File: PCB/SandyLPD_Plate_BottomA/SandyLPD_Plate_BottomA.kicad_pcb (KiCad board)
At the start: 2 copper layers, 127.4 x 83 mm, 14 parts

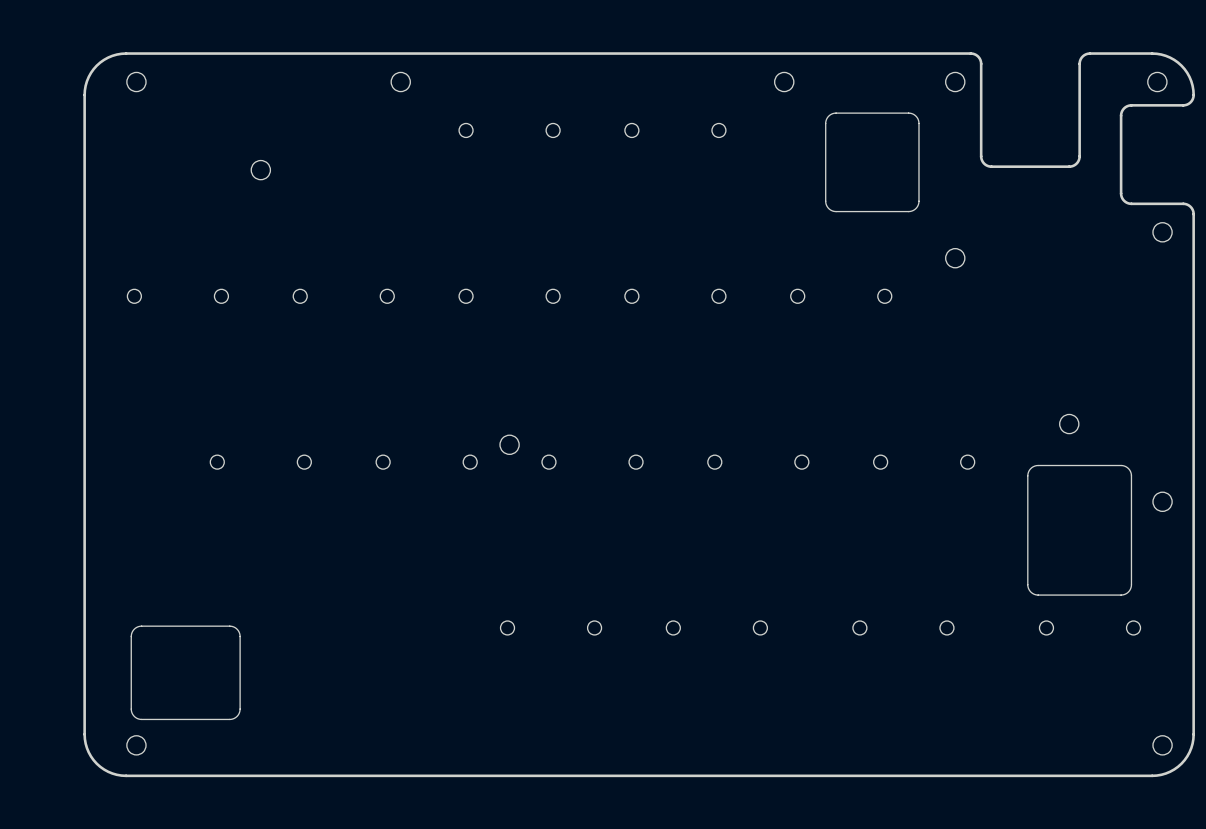
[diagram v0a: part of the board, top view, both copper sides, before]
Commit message: ボトムプレートの外形を、基板Baseと同形状に戻す。
仕様では左右端を斜めにして、テント時の小指側持ち上がりを防止する予定だった。
しかし、ケースなどを考慮すると、ボトムの外形が異なると不都合なため、基板Baseと同形状とする。
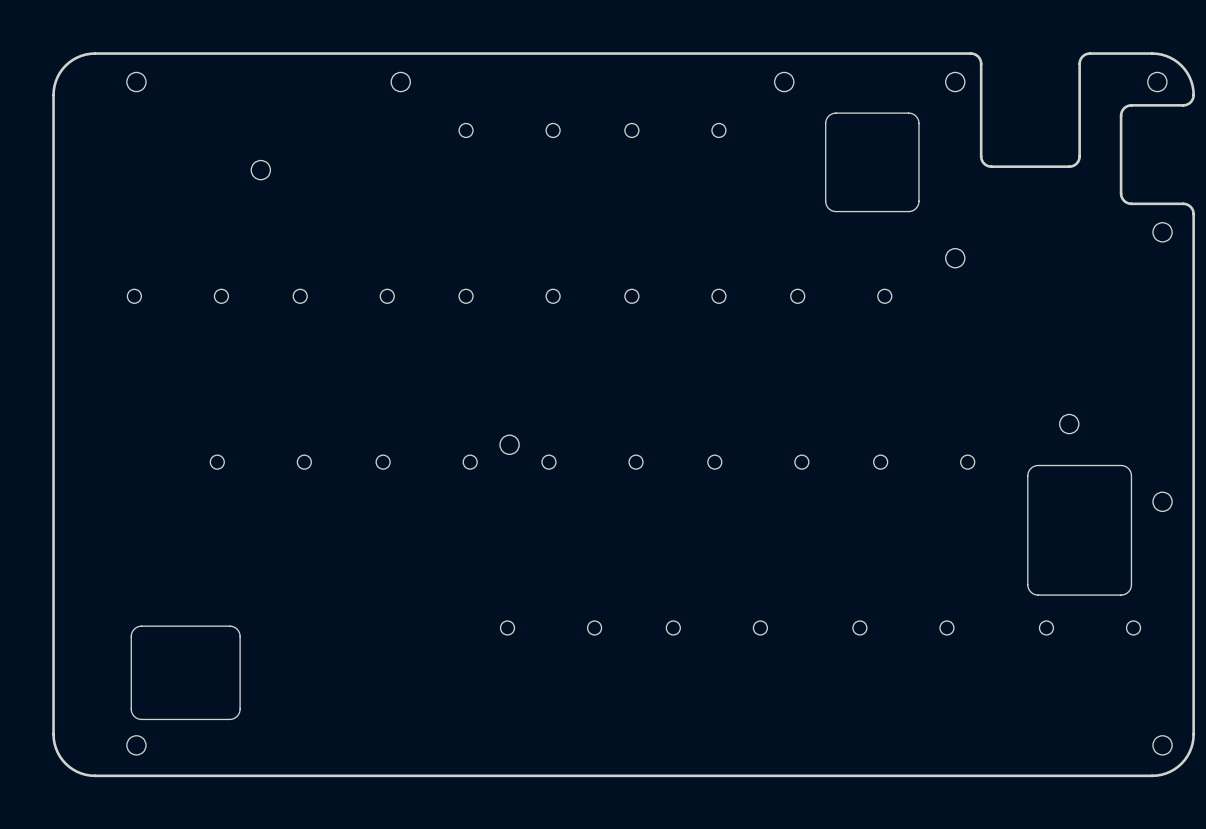
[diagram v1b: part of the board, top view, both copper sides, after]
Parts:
- REF**: footprint locallib:SandyLP-Duo_outline_BottomA_narrow_edge -> locallib:SandyLP-Duo_outline_BottomA
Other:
- board size 127.4 x 83 mm -> 131 x 83 mm
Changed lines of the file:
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@@
 		)
 	)
-	(footprint "locallib:SandyLP-Duo_outline_BottomA_narrow_edge"
+	(footprint "locallib:SandyLP-Duo_outline_BottomA"
 		(locked yes)
 		(layer "F.Cu")
@@
 			)
 		)
-		(property "Footprint" "locallib:SandyLP-Duo_outline_BottomA_narrow_edge"
+		(property "Footprint" "locallib:SandyLP-Duo_outline_BottomA"
 			(at 2.38125 0 0)
 			(layer "F.Fab")
@@
 		)
 		(property "LCSC-Reserve" ""
-			(at 125.015625 11.015585 0)
+			(at -97.63125 19.05 90)
 			(unlocked yes)
 			(layer "B.Fab")
@@
 		)
 		(property "text" "RESET"
-			(at 127.015625 12.715585 0)
+			(at -97.63125 22.50661 180)
 			(unlocked yes)
 			(layer "B.SilkS")
@@
 			(effects
 				(font
-					(size 0.8 0.8)
-					(thickness 0.12)
+					(size 1 1)
+					(thickness 0.15)
 				)
-				(justify right mirror)
+				(justify mirror)
 			)
 		)
@@
 			)
 		)
-		(attr through_hole)
+		(attr through_hole board_only)
 		(fp_line
 			(start -140.49375 -66.675)
@@
 		)
 		(fp_line
-			(start -132.159486 26.123471)
-			(end -132.159486 -47.32504)
+			(start -135.731364 26.123471)
+			(end -135.731364 -47.32504)
 			(stroke
 				(width 0.3)
@@
 		(fp_line
 			(start -30.360962 -52.08754)
-			(end -127.396986 -52.08754)
+			(end -130.968864 -52.08754)
 			(stroke
 				(width 0.3)
@@
 		(fp_line
 			(start -9.525004 30.885971)
-			(end -127.396986 30.885971)
+			(end -130.968864 30.885971)
 			(stroke
 				(width 0.3)
@@
 		)
 		(fp_arc
-			(start -132.159486 -47.32504)
-			(mid -130.764582 -50.692636)
-			(end -127.396986 -52.08754)
+			(start -135.731364 -47.32504)
+			(mid -134.33646 -50.692636)
+			(end -130.968864 -52.08754)
 			(stroke
 				(width 0.3)
@@
 		)
 		(fp_arc
-			(start -127.396986 30.885971)
-			(mid -130.764582 29.491067)
-			(end -132.159486 26.123471)
+			(start -130.968864 30.885971)
+			(mid -134.33646 29.491067)
+			(end -135.731364 26.123471)
 			(stroke
 				(width 0.3)
@@
 		)
 		(group ""
-			(members "005edbd5-9dcd-470a-a973-d1f1d2a61a1a" "05d2eae7-c181-422d-9569-904796de0269"
-				"9b183af6-5e10-4e59-8052-0b5744671b76" "b55f851b-591d-4a62-a20e-bd009cb65a13"
-			)
-		)
-		(group ""
-			(members "42a0653b-d340-4603-a827-220ef89f28cc" "850d6d43-24ba-41c6-9baf-5d99699f05ff")
-		)
-		(group ""
-			(members "00bba4d7-927c-44bf-abe4-f5398d7c5d70" "3fc21fe5-b83e-4190-8479-5b87a99d230f"
-				"5695b5e9-40c7-4808-97a4-c3f6905e49b1" "98fb170c-914d-4c2a-b8dc-1b4193d5b75c"
-			)
-		)
-		(group ""
-			(members "2114cb56-aaf9-424c-958d-764355443606" "22d33ce8-87ca-4359-a9de-ef28831f7c19"
-				"351bab31-3389-412d-acae-cb307b4c7e3e" "eb69ca11-c496-4460-b676-2f4452785759"
-			)
-		)
-		(group ""
-			(members "0047b21b-dea4-4b7c-ad55-e57c259c307c" "29b073e0-2a04-4572-8567-e3811bda6a15"
-				"77b25d4e-8323-4d78-971c-3cebbb8b50fd"
-			)
-		)
-		(group ""
-			(members "30b09278-b5c3-452a-9b74-d88fc7e4de33" "9bb58a16-0232-48a8-8b61-7405ef1a8437"
-				"c234e008-7641-4094-bf84-fe76896330e9"
-			)
-		)
-		(group ""
-			(members "27051af8-4828-47fd-bd2c-5783529d2d3c" "4f6412f7-2e76-4052-b919-9ae8df068e09"
-				"da862006-59d0-48f0-af84-c2b3950611b3"
-			)
-		)
-		(group ""
-			(members "4e68ace4-0a08-4553-a9ea-0aca04e8a678" "8083394e-fa4c-4ab0-9e85-c20af4f6b881"
-				"f871543f-5335-4d4e-a8c8-eb321251eed3"
-			)
-		)
-		(group ""
-			(members "162c7e05-0cab-437d-964e-3a034e5c93db" "27b03c83-74c5-462a-8bb9-f4302292ff28"
-				"94b7f3ef-9673-44e5-82e3-eb0b3f6f3867"
-			)
-		)
-		(group ""
-			(members "83e13a7e-7942-444c-b689-bfa5e10521b8" "8f398c76-707b-4463-be56-22b0d8080667"
-				"e7605193-7462-471f-979d-74e4487fd460"
-			)
-		)
-		(group ""
-			(members "4f8089c0-3afb-49d3-8d5a-00519c085a6d" "657a6b24-7aa7-4307-ab6f-31d937f6afff"
-				"c17c0421-2946-4162-9b96-5a1f954f5d27"
-			)
-		)
-		(group ""
-			(members "20ce9a84-afb0-4c77-b779-3d139d9c7c1d" "a4a9556f-885c-41b6-bd16-850c0e5a4910"
-				"c1f55ea5-07ff-4878-bbb3-28cd7b18d6e4"
-			)
-		)
-		(group ""
-			(members "990a4551-984d-4bbe-8049-91a3043cd0b8" "cf7cfe3b-81bb-490e-85b5-f96267643e1b"
-				"f8a0acfc-dc36-4631-84b4-7c14b025cac1"
-			)
-		)
-		(group ""
-			(members "71f33917-bf52-475a-96be-18edf2ad2e9b" "c20582ea-7f0c-447c-91e7-f06e8854089a"
-				"e2f5758b-f261-41e1-bf9b-ea9e8c73e7c5"
-			)
-		)
-		(group ""
-			(members "24957f64-19f9-4ebe-af70-10ff27c7b894" "5c667c15-8fa1-40d5-8bb5-5f8ca7b33a4f"
-				"bde45b41-1ed9-4ff2-a4a1-598ec35577d0"
-			)
-		)
-		(group ""
-			(members "4b262687-535b-4b71-b50e-c1b3c09d4763" "6457ffeb-18c2-4019-942c-4b4097e8bd1e"
-				"7a08e892-188a-4d2b-b535-3c2151e6a3cb"
-			)
-		)
-		(group ""
-			(members "0ba3edbb-be55-4cc1-8689-aa70d6c0190d" "653fb40f-2811-46bd-a5b8-fef2f5af4ec3"
-				"f404e5fb-4055-419b-a6f1-4105c89f8d55"
-			)
-		)
-		(group ""
-			(members "09f0a9b0-09f9-4392-8691-bb053f5843d8" "346f39a6-52ef-4b8d-b4cc-c828106052b7"
-				"4f1562ec-583d-4b9e-913d-2068b0b31fe3" "9f233960-38e7-4d17-8b07-61f26d310015"
-				"a5ed21ac-c260-4b32-9b59-175a99054753" "ceb8e2f6-c06f-4b01-ac69-351496e250e1"
-				"fc590dfd-88df-4a9d-94aa-c44babb90b2a"
-			)
-		)
+			(members "768d52e1-6995-4e07-a8f7-905398240928" "7c9ff0f7-4d82-402f-bc0a-521dbdc4ffab"
+				"c7a505ad-1373-40c9-8598-3adb5f37292c" "d3a47df1-53fc-47b6-bce4-7b199c321008"
+			)
+		)
+		(group ""
+			(members "27b3e30e-4b55-4486-b54d-d5f02c1e864f" "47688318-7972-4377-adad-ed33bbecca86"
+				"61592db4-dc05-4c05-867c-43a3c4575e85" "ab165d60-8426-4dda-93f6-c43c93c70db7"
+			)
+		)
+		(group ""
+			(members "050ef1a6-a3f2-433d-ba6f-f7bf6cbc7701" "266b9d01-f5d8-45c4-a070-ecec62cbbcd0"
+				"3fd5bdf2-c0fe-45b4-ab12-3b4e4d8df1f7" "6698c4d4-7943-4c04-8872-1a55fe845aab"
+			)
+		)
+		(group ""
+			(members "120b0628-372f-493f-b00e-15f3ba5435f2" "b84d7721-bd67-439d-8f72-ec4f61046289")
+		)
+		(group ""
+			(members "0b69fad6-0d2d-46c8-8b7f-c6ae73ae9535" "330257f5-ee5d-4c76-80d8-5f791fdf178f"
+				"e02aad9b-a0a9-48c2-aac7-61630aa05e4b"
+			)
+		)
+		(group ""
+			(members "0a2b1baf-e4ce-4170-b5fe-0cd55f32a29b" "4c80776c-a1aa-4eac-a4f0-7c2fa99df76c"
+				"9b2fab13-b30c-465b-b73c-f1cb87b9b07d"
+			)
+		)
+		(group ""
+			(members "3cc7c1a2-46e7-43fa-8d77-b0583e360804" "9993816f-2ec5-4f18-8ccb-fa76e125fbf3"
+				"c0989285-ddbc-48e9-bfa8-efb41389e4ee"
+			)
+		)
+		(group ""
+			(members "6a4246bb-16fd-4932-8b00-0759913a3d4d" "7369f70d-806d-4907-98e3-015ef96cb96d"
+				"7bb1f348-f5a8-4d84-aa64-cfe7065df81c"
+			)
+		)
+		(group ""
+			(members "2cd84ebf-6e32-4566-8d34-cbd5c0dce843" "ac2ea378-a8dc-4c2b-8970-88981ff65753"
+				"b4734dbe-c653-43f4-8039-96a65bf3900d"
+			)
+		)
+		(group ""
+			(members "12e533cc-6258-43f2-9c2e-665cb9adc7f7" "1f986533-4d05-4a11-9c0a-8a3708b5372b"
+				"931a2f65-5bcb-44d3-b7dd-751c7b60f58b"
+			)
+		)
+		(group ""
+			(members "2611aa98-c19b-4191-9a14-da2c351c2c8c" "7c83b1d8-b4a3-49de-83ec-d4ebc99a612e"
+				"c12838cb-8578-4aa5-b47d-60ebd0292c47"
+			)
+		)
+		(group ""
+			(members "af508a5a-8108-4dad-8260-e2b96960a5a1" "af604911-4095-4891-a997-ae5661578ee4"
+				"dacfb637-0ed1-493e-93e5-c88e1ac657cb"
+			)
+		)
+		(group ""
+			(members "127c6c8f-8dc6-4082-9bb4-d7a6a6d983af" "1365b648-5cb8-4079-bcc7-22ed2e8a1f14"
+				"f56c55e2-61a0-4616-9f47-95582bca677a"
+			)
+		)
+		(group ""
+			(members "5a9f1272-29aa-498f-aac3-a79cfba13a0f" "8d27a991-15c2-4cf6-8f08-53455c4a44d3"
+				"bcdf979c-70a9-4690-9902-d5d13f43a3ff"
+			)
+		)
+		(group ""
+			(members "341c500e-d4b8-4c4d-aff6-785cf25e11de" "44107841-d251-407a-9a46-594b2a54cde6"
+				"86f19132-709f-4b84-827d-3de39abfd1b1"
+			)
+		)
+		(group ""
+			(members "5b0d7b5c-7741-4c0a-83dd-f11fbcda69bb" "638280cb-4e4f-4d5d-a0ad-a617928cc635"
+				"96436da2-e83e-4c46-a5ea-b19277da9758"
+			)
+		)
+		(group ""
+			(members "1fb38e07-3180-42ea-b84e-b8959f434f60" "af95d0d9-5dfa-4313-b6c6-74592eeea5cf"
+				"bb264223-f065-43ed-a360-1068521864a8"
+			)
+		)
+		(group ""
+			(members "099a1441-f742-4c18-bcac-b4f41b16570d" "1c8e6033-ca91-4b2b-90ca-e53cea9a4255"
+				"1cbb4c32-75d4-4e97-a4f2-0c4f3be2bba7" "5f7d4a69-8910-41d2-a414-02484530e2fb"
+				"99a17b21-8b5f-46dc-8c4d-2b70c8e77b8d" "ac859754-1366-4110-973d-db881cdbc23a"
+				"c2c4e08e-bcca-4d8f-ab7d-31ca58c78905"
+			)
+		)

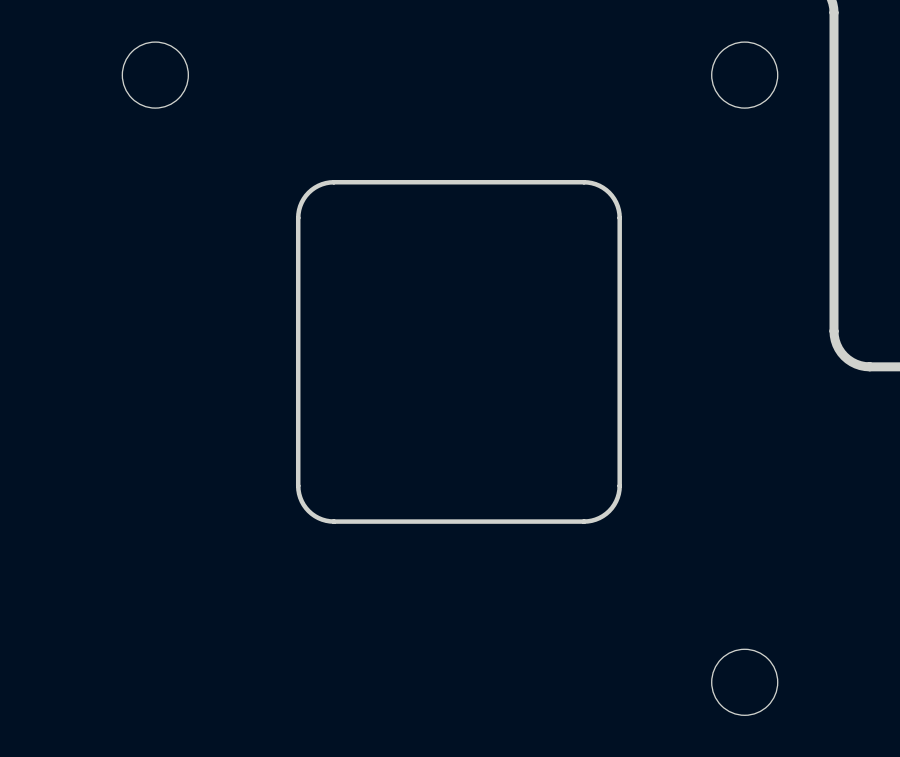
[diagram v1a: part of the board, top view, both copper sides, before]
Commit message: 部品逃がし穴の位置とサイズを調整
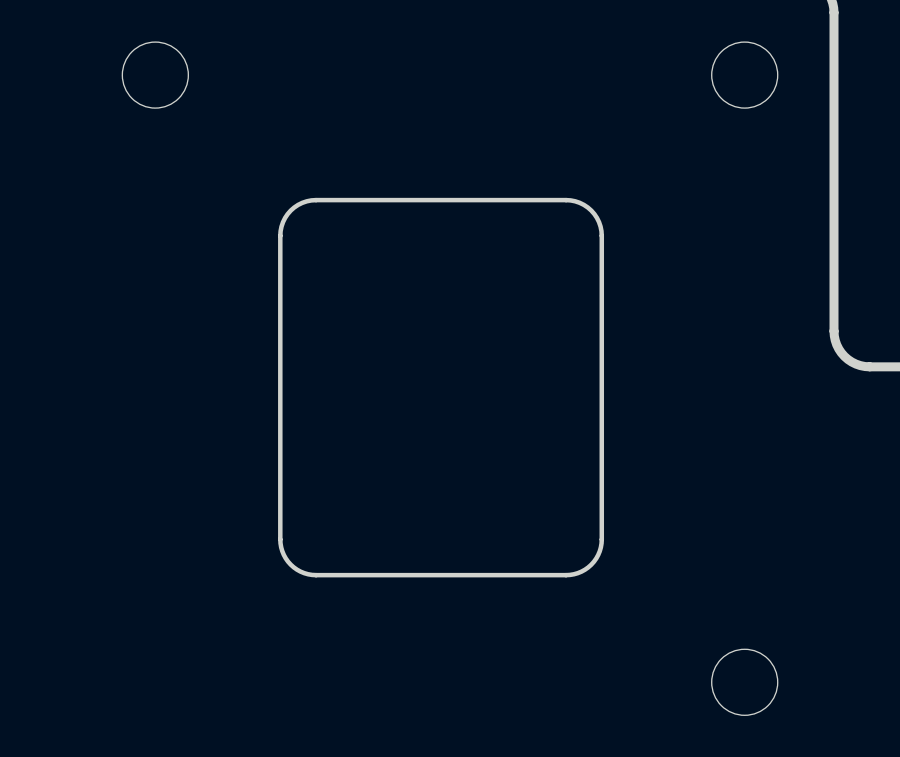
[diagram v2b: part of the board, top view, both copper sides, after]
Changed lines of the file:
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@@
+		(layer "Eco2.User")
+	)
+	(gr_rect
+		(start 111.543804 39.50499)
+		(end 122.259477 51.41125)
+		(stroke
+			(width 0.1)
+			(type default)
+		)
+		(fill none)
 		(layer "Eco2.User")
 	)
@@
 		(layer "Edge.Cuts")
 	)
-	(gr_line
-		(start 112.141322 40.100289)
-		(end 112.141322 49.029984)
-		(locked yes)
-		(stroke
-			(width 0.15)
-			(type default)
-		)
-		(layer "Edge.Cuts")
-	)
-	(gr_line
-		(start 122.856956 49.029984)
-		(end 122.856956 40.100289)
-		(locked yes)
-		(stroke
-			(width 0.15)
-			(type default)
-		)
-		(layer "Edge.Cuts")
-	)
 	(gr_arc
 		(start 147.264789 93.083146)
@@
 		(layer "Edge.Cuts")
 	)
-	(gr_arc
-		(start 112.141322 40.100289)
-		(mid 112.490048 39.258389)
-		(end 113.331948 38.909663)
-		(locked yes)
-		(stroke
-			(width 0.15)
-			(type default)
-		)
-		(layer "Edge.Cuts")
-	)
-	(gr_arc
-		(start 121.66633 38.909663)
-		(mid 122.50823 39.258389)
-		(end 122.856956 40.100289)
-		(locked yes)
-		(stroke
-			(width 0.15)
-			(type default)
-		)
-		(layer "Edge.Cuts")
-	)
-	(gr_line
-		(start 121.66633 50.22061)
-		(end 113.331948 50.22061)
+	(gr_line
+		(start 122.259611 40.695531)
+		(end 122.259611 50.815579)
+		(locked yes)
+		(stroke
+			(width 0.15)
+			(type default)
+		)
+		(layer "Edge.Cuts")
+	)
+	(gr_arc
+		(start 111.543977 40.695531)
+		(mid 111.89271 39.853655)
+		(end 112.734603 39.504905)
+		(locked yes)
+		(stroke
+			(width 0.15)
+			(type default)
+		)
+		(layer "Edge.Cuts")
+	)
+	(gr_arc
+		(start 121.068985 39.504905)
+		(mid 121.910869 39.853641)
+		(end 122.259611 40.695531)
+		(locked yes)
+		(stroke
+			(width 0.15)
+			(type default)
+		)
+		(layer "Edge.Cuts")
+	)
+	(gr_line
+		(start 121.068985 52.006205)
+		(end 112.734603 52.006205)
 		(locked yes)
 		(stroke
@@
 	)
 	(gr_arc
-		(start 122.856956 49.029984)
-		(mid 122.50823 49.871884)
-		(end 121.66633 50.22061)
+		(start 122.259611 50.815579)
+		(mid 121.910892 51.6575)
+		(end 121.068985 52.006205)
 		(locked yes)
 		(stroke
@@
 		(start 32.36938 99.036276)
 		(end 32.36938 107.370658)
+		(locked yes)
+		(stroke
+			(width 0.15)
+			(type default)
+		)
+		(layer "Edge.Cuts")
+	)
+	(gr_line
+		(start 111.543977 50.815579)
+		(end 111.543977 40.695531)
 		(locked yes)
 		(stroke
@@
 	)
 	(gr_line
-		(start 113.331948 38.909663)
-		(end 121.66633 38.909663)
-		(locked yes)
-		(stroke
-			(width 0.15)
-			(type default)
-		)
-		(layer "Edge.Cuts")
-	)
-	(gr_arc
-		(start 113.331948 50.22061)
-		(mid 112.490048 49.871884)
-		(end 112.141322 49.029984)
+		(start 112.734603 39.504905)
+		(end 121.068985 39.504905)
+		(locked yes)
+		(stroke
+			(width 0.15)
+			(type default)
+		)
+		(layer "Edge.Cuts")
+	)
+	(gr_arc
+		(start 112.734603 52.006205)
+		(mid 111.892678 51.657495)
+		(end 111.543977 50.815579)
 		(locked yes)
 		(stroke
@@
 	(group ""
 		(locked yes)
-		(members "14a750f5-06af-4e89-880a-e590238e0df6" "15208253-21da-46c6-a8ff-613fe04e41f9"
-			"2f344255-e197-4630-81c6-211e9e54db80" "35058d3e-8c33-4cf1-9c07-fe359fc8d885"
-			"3c740912-60f8-4a88-a299-76d2614c6534" "51eed6f2-81d0-4c08-ac7e-b058e24c4508"
+		(members "2cccd29b-8648-4d96-829c-5fee96896f34" "2f344255-e197-4630-81c6-211e9e54db80"
+			"35058d3e-8c33-4cf1-9c07-fe359fc8d885" "3c740912-60f8-4a88-a299-76d2614c6534"
+			"51eed6f2-81d0-4c08-ac7e-b058e24c4508" "5e029abe-d5aa-4767-806d-414a694131e1"
 			"863fb807-8d86-4189-a670-b5aee21a557d" "94a5de24-bdad-4ae1-8b7c-cd8fb626c9a5"
 		)
